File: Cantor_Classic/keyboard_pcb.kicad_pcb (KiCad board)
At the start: 2 copper layers, 138.8 x 89.9 mm, 23 parts, among them J1 TRRS, K00 KEYSW, K01 KEYSW, K02 KEYSW, K03 KEYSW, K04 KEYSW, K05 KEYSW, K10 KEYSW, K11 KEYSW, K12 KEYSW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

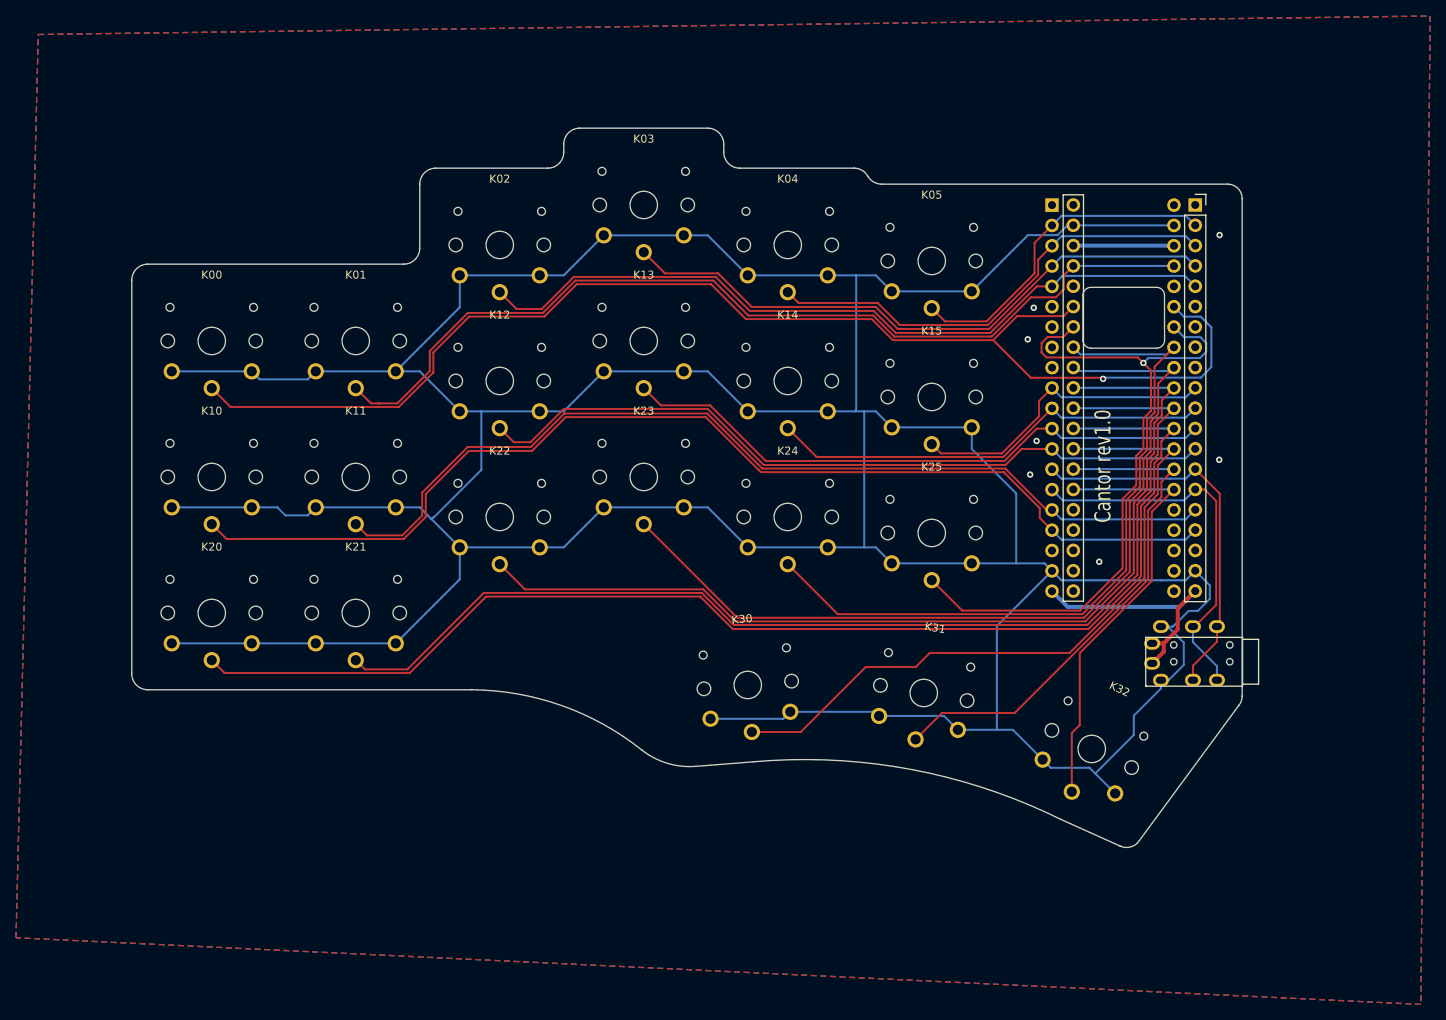
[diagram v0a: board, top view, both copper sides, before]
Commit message: [V1] Mounting holes
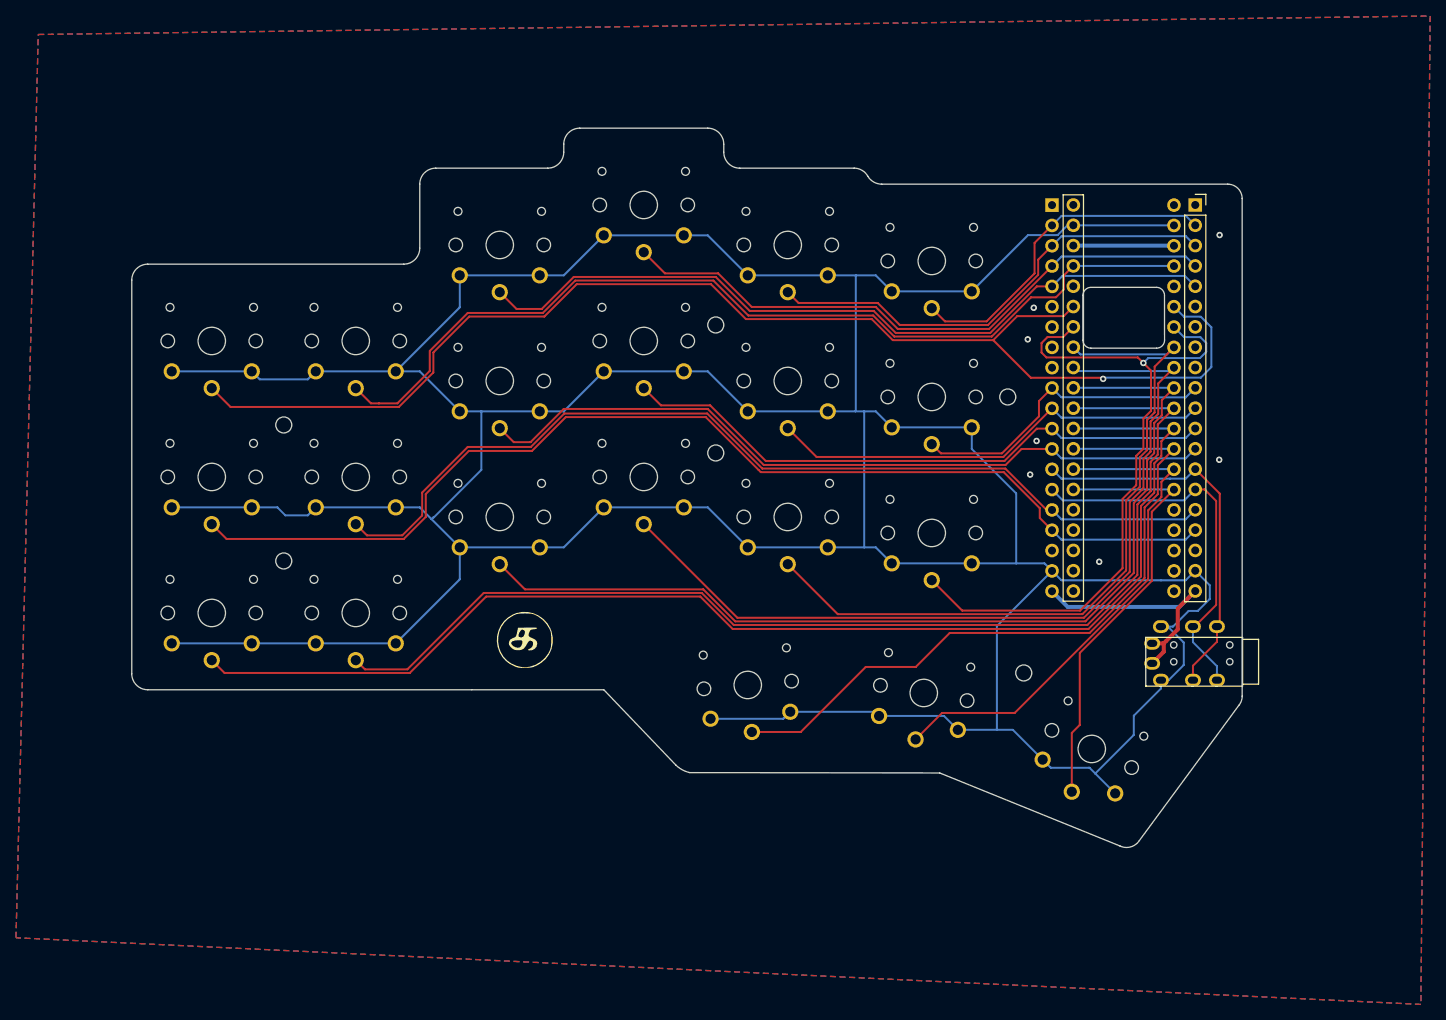
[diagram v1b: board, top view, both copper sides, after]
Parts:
- added G***: LOGO, kdkb_tools:logo-small, F.Cu at (113.0, 107.5)
- added G***: LOGO, kdkb_tools:logo-small, B.Cu at (113.0, 107.5)
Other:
- outline, holes or cut-outs redrawn
- board text removed: "Cantor"
- board text removed: "Cantor rev1.0"
